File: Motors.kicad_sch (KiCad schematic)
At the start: 0 parts

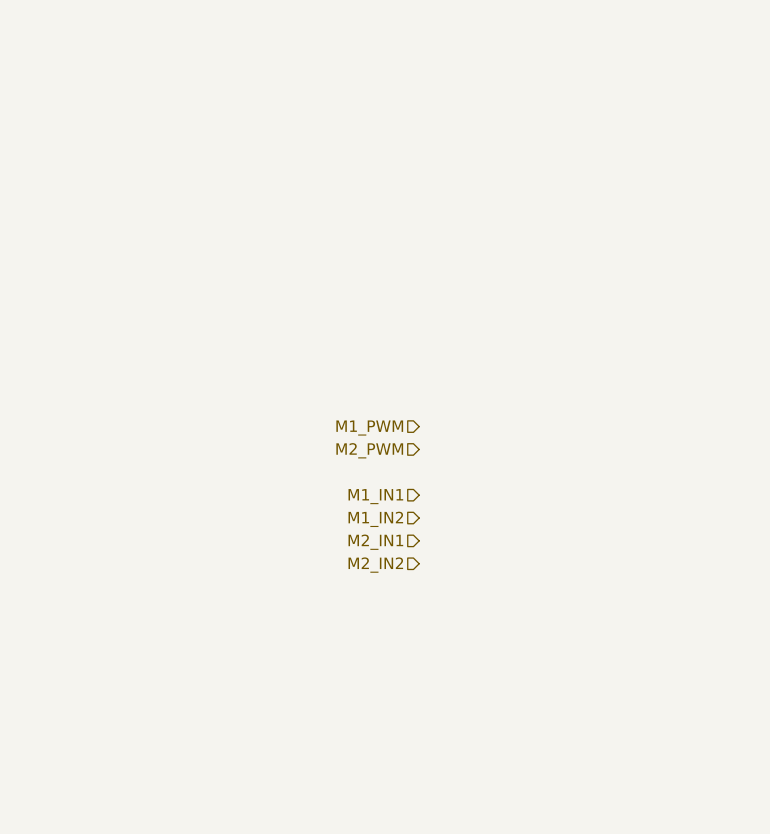
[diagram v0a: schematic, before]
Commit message: Motors schematic
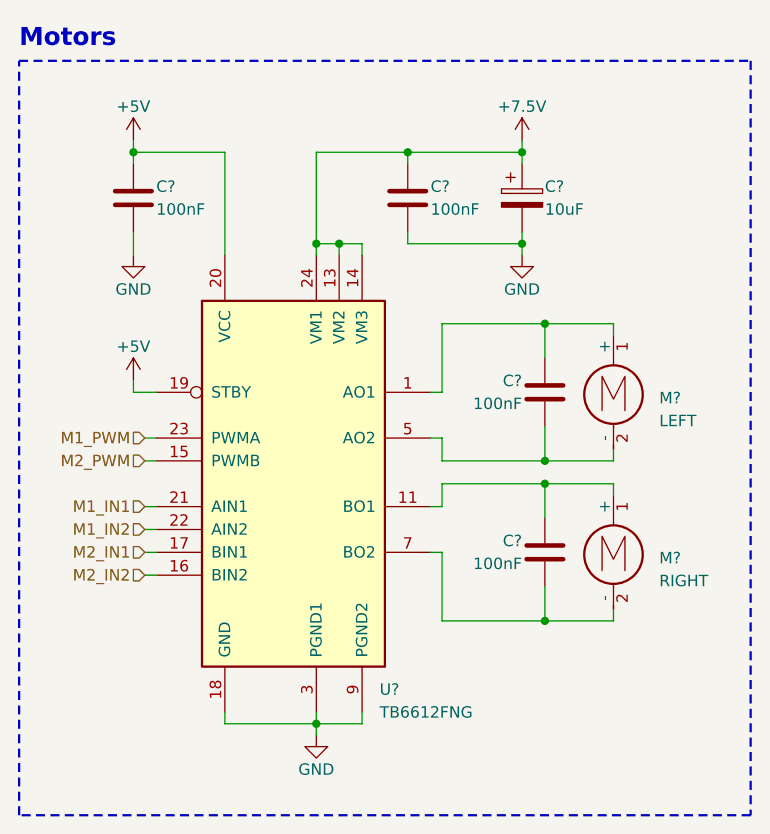
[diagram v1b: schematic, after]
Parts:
- added C? (x4): 100nF, symbol Device:C
- added C?: 10uF, symbol Device:C_Polarized
- added M?: RIGHT, symbol Motor:Motor_DC
- added M?: LEFT, symbol Motor:Motor_DC
- added U?: TB6612FNG, Package_SO:SSOP-24_5.3x8.2mm_P0.65mm, symbol Driver_Motor:TB6612FNG
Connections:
- net M1_IN1: now also U?.21 (AIN1)
- net M1_IN2: now also U?.22 (AIN2)
- net M1_PWM: now also U?.23 (PWMA)
- net M2_IN1: now also U?.17 (BIN1)
- net M2_IN2: now also U?.16 (BIN2)
- net M2_PWM: now also U?.15 (PWMB)
- new net: C?.1, M?.1 (+), U?.11 (BO1), U?.12 (BO1)
- new net: C?.2, M?.2 (-), U?.7 (BO2), U?.8 (BO2)
- new net: C?.1, M?.1 (+), U?.1 (AO1), U?.2 (AO1)
- new net: C?.2, M?.2 (-), U?.5 (AO2), U?.6 (AO2)
- new net +5V: C?.1, U?.19 (STBY), U?.20 (VCC)
- new net +7.5V: C?.1, C?.1, U?.13 (VM2), U?.14 (VM3), U?.24 (VM1)
- new net GND: C?.2, C?.2, C?.2, U?.10 (PGND2), U?.18 (GND), U?.3 (PGND1), U?.4 (PGND1), U?.9 (PGND2)
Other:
- note added: "Motors"

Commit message: Annotate schematics
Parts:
- gave numbers to parts that had none: 8
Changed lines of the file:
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@@
   (symbol (lib_id "power:+5V") (at 34.29 31.75 0) (unit 1)
     (in_bom yes) (on_board yes) (dnp no) (fields_autoplaced)
-    (property "Reference" "#PWR032" (at 34.29 35.56 0)
+    (property "Reference" "#PWR048" (at 34.29 35.56 0)
       (effects (font (size 1.27 1.27)) hide)
     )
@@
       (project "Autko"
         (path "/8d5cfdec-de34-4148-9100-7125640c46f5/541574ca-21e4-445f-b8e2-ded2c59d3b8a"
-          (reference "#PWR032") (unit 1)
+          (reference "#PWR048") (unit 1)
         )
       )
@@
   (symbol (lib_id "Motor:Motor_DC") (at 87.63 76.2 0) (unit 1)
     (in_bom yes) (on_board yes) (dnp no) (fields_autoplaced)
-    (property "Reference" "M?" (at 92.71 78.105 0)
+    (property "Reference" "M2" (at 92.71 78.105 0)
       (effects (font (size 1.27 1.27)) (justify left))
     )
@@
       (project "Autko"
         (path "/8d5cfdec-de34-4148-9100-7125640c46f5/541574ca-21e4-445f-b8e2-ded2c59d3b8a"
-          (reference "M?") (unit 1)
+          (reference "M2") (unit 1)
         )
       )
@@
   (symbol (lib_id "power:+5V") (at 34.29 58.42 0) (unit 1)
     (in_bom yes) (on_board yes) (dnp no) (fields_autoplaced)
-    (property "Reference" "#PWR025" (at 34.29 62.23 0)
+    (property "Reference" "#PWR052" (at 34.29 62.23 0)
       (effects (font (size 1.27 1.27)) hide)
     )
@@
       (project "Autko"
         (path "/8d5cfdec-de34-4148-9100-7125640c46f5/541574ca-21e4-445f-b8e2-ded2c59d3b8a"
-          (reference "#PWR025") (unit 1)
+          (reference "#PWR052") (unit 1)
         )
       )
@@
   (symbol (lib_id "Device:C") (at 34.29 38.1 0) (unit 1)
     (in_bom yes) (on_board yes) (dnp no)
-    (property "Reference" "C?" (at 36.83 36.83 0)
+    (property "Reference" "C21" (at 36.83 36.83 0)
       (effects (font (size 1.27 1.27)) (justify left))
     )
@@
       (project "Autko"
         (path "/8d5cfdec-de34-4148-9100-7125640c46f5/541574ca-21e4-445f-b8e2-ded2c59d3b8a"
-          (reference "C?") (unit 1)
+          (reference "C21") (unit 1)
         )
       )
@@
   (symbol (lib_id "Device:C") (at 80.01 77.47 0) (mirror y) (unit 1)
     (in_bom yes) (on_board yes) (dnp no)
-    (property "Reference" "C?" (at 77.47 76.2 0)
+    (property "Reference" "C25" (at 77.47 76.2 0)
       (effects (font (size 1.27 1.27)) (justify left))
     )
@@
       (project "Autko"
         (path "/8d5cfdec-de34-4148-9100-7125640c46f5/541574ca-21e4-445f-b8e2-ded2c59d3b8a"
-          (reference "C?") (unit 1)
+          (reference "C25") (unit 1)
         )
       )
@@
   (symbol (lib_id "Driver_Motor:TB6612FNG") (at 52.07 69.85 0) (unit 1)
     (in_bom yes) (on_board yes) (dnp no) (fields_autoplaced)
-    (property "Reference" "U?" (at 61.6459 92.71 0)
+    (property "Reference" "U12" (at 61.6459 92.71 0)
       (effects (font (size 1.27 1.27)) (justify left))
     )
@@
       (project "Autko"
         (path "/8d5cfdec-de34-4148-9100-7125640c46f5/541574ca-21e4-445f-b8e2-ded2c59d3b8a"
-          (reference "U?") (unit 1)
+          (reference "U12") (unit 1)
         )
       )
@@
   (symbol (lib_id "power:GND") (at 77.47 44.45 0) (unit 1)
     (in_bom yes) (on_board yes) (dnp no)
-    (property "Reference" "#PWR044" (at 77.47 50.8 0)
+    (property "Reference" "#PWR051" (at 77.47 50.8 0)
       (effects (font (size 1.27 1.27)) hide)
     )
@@
       (project "Autko"
         (path "/8d5cfdec-de34-4148-9100-7125640c46f5/541574ca-21e4-445f-b8e2-ded2c59d3b8a"
-          (reference "#PWR044") (unit 1)
+          (reference "#PWR051") (unit 1)
         )
       )
@@
   (symbol (lib_id "power:+7.5V") (at 77.47 31.75 0) (unit 1)
     (in_bom yes) (on_board yes) (dnp no) (fields_autoplaced)
-    (property "Reference" "#PWR033" (at 77.47 35.56 0)
+    (property "Reference" "#PWR049" (at 77.47 35.56 0)
       (effects (font (size 1.27 1.27)) hide)
     )
@@
       (project "Autko"
         (path "/8d5cfdec-de34-4148-9100-7125640c46f5/541574ca-21e4-445f-b8e2-ded2c59d3b8a"
-          (reference "#PWR033") (unit 1)
+          (reference "#PWR049") (unit 1)
         )
       )
@@
   (symbol (lib_id "Device:C") (at 80.01 59.69 0) (mirror y) (unit 1)
     (in_bom yes) (on_board yes) (dnp no)
-    (property "Reference" "C?" (at 77.47 58.42 0)
+    (property "Reference" "C24" (at 77.47 58.42 0)
       (effects (font (size 1.27 1.27)) (justify left))
     )
@@
       (project "Autko"
         (path "/8d5cfdec-de34-4148-9100-7125640c46f5/541574ca-21e4-445f-b8e2-ded2c59d3b8a"
-          (reference "C?") (unit 1)
+          (reference "C24") (unit 1)
         )
       )
@@
   (symbol (lib_id "Device:C") (at 64.77 38.1 0) (unit 1)
     (in_bom yes) (on_board yes) (dnp no)
-    (property "Reference" "C?" (at 67.31 36.83 0)
+    (property "Reference" "C22" (at 67.31 36.83 0)
       (effects (font (size 1.27 1.27)) (justify left))
     )
@@
       (project "Autko"
         (path "/8d5cfdec-de34-4148-9100-7125640c46f5/541574ca-21e4-445f-b8e2-ded2c59d3b8a"
-          (reference "C?") (unit 1)
+          (reference "C22") (unit 1)
         )
       )
@@
   (symbol (lib_id "power:GND") (at 34.29 44.45 0) (unit 1)
     (in_bom yes) (on_board yes) (dnp no)
-    (property "Reference" "#PWR026" (at 34.29 50.8 0)
+    (property "Reference" "#PWR050" (at 34.29 50.8 0)
       (effects (font (size 1.27 1.27)) hide)
     )
@@
       (project "Autko"
         (path "/8d5cfdec-de34-4148-9100-7125640c46f5/541574ca-21e4-445f-b8e2-ded2c59d3b8a"
-          (reference "#PWR026") (unit 1)
+          (reference "#PWR050") (unit 1)
         )
       )
@@
   (symbol (lib_id "power:GND") (at 54.61 97.79 0) (unit 1)
     (in_bom yes) (on_board yes) (dnp no)
-    (property "Reference" "#PWR045" (at 54.61 104.14 0)
+    (property "Reference" "#PWR053" (at 54.61 104.14 0)
       (effects (font (size 1.27 1.27)) hide)
     )
@@
       (project "Autko"
         (path "/8d5cfdec-de34-4148-9100-7125640c46f5/541574ca-21e4-445f-b8e2-ded2c59d3b8a"
-          (reference "#PWR045") (unit 1)
+          (reference "#PWR053") (unit 1)
         )
       )
@@
   (symbol (lib_id "Device:C_Polarized") (at 77.47 38.1 0) (unit 1)
     (in_bom yes) (on_board yes) (dnp no)
-    (property "Reference" "C?" (at 80.01 36.83 0)
+    (property "Reference" "C23" (at 80.01 36.83 0)
       (effects (font (size 1.27 1.27)) (justify left))
     )
@@
       (project "Autko"
         (path "/8d5cfdec-de34-4148-9100-7125640c46f5/541574ca-21e4-445f-b8e2-ded2c59d3b8a"
-          (reference "C?") (unit 1)
+          (reference "C23") (unit 1)
         )
       )
@@
   (symbol (lib_id "Motor:Motor_DC") (at 87.63 58.42 0) (unit 1)
     (in_bom yes) (on_board yes) (dnp no) (fields_autoplaced)
-    (property "Reference" "M?" (at 92.71 60.325 0)
+    (property "Reference" "M1" (at 92.71 60.325 0)
       (effects (font (size 1.27 1.27)) (justify left))
     )
@@
       (project "Autko"
         (path "/8d5cfdec-de34-4148-9100-7125640c46f5/541574ca-21e4-445f-b8e2-ded2c59d3b8a"
-          (reference "M?") (unit 1)
-        )
-      )
+          (reference "M1") (unit 1)
+        )
+      )
